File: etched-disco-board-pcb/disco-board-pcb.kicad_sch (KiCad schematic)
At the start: 15 parts, among them J1 Conn_02x32_Odd_Even, J2 Conn_02x32_Odd_Even, U2 MMA8452Q

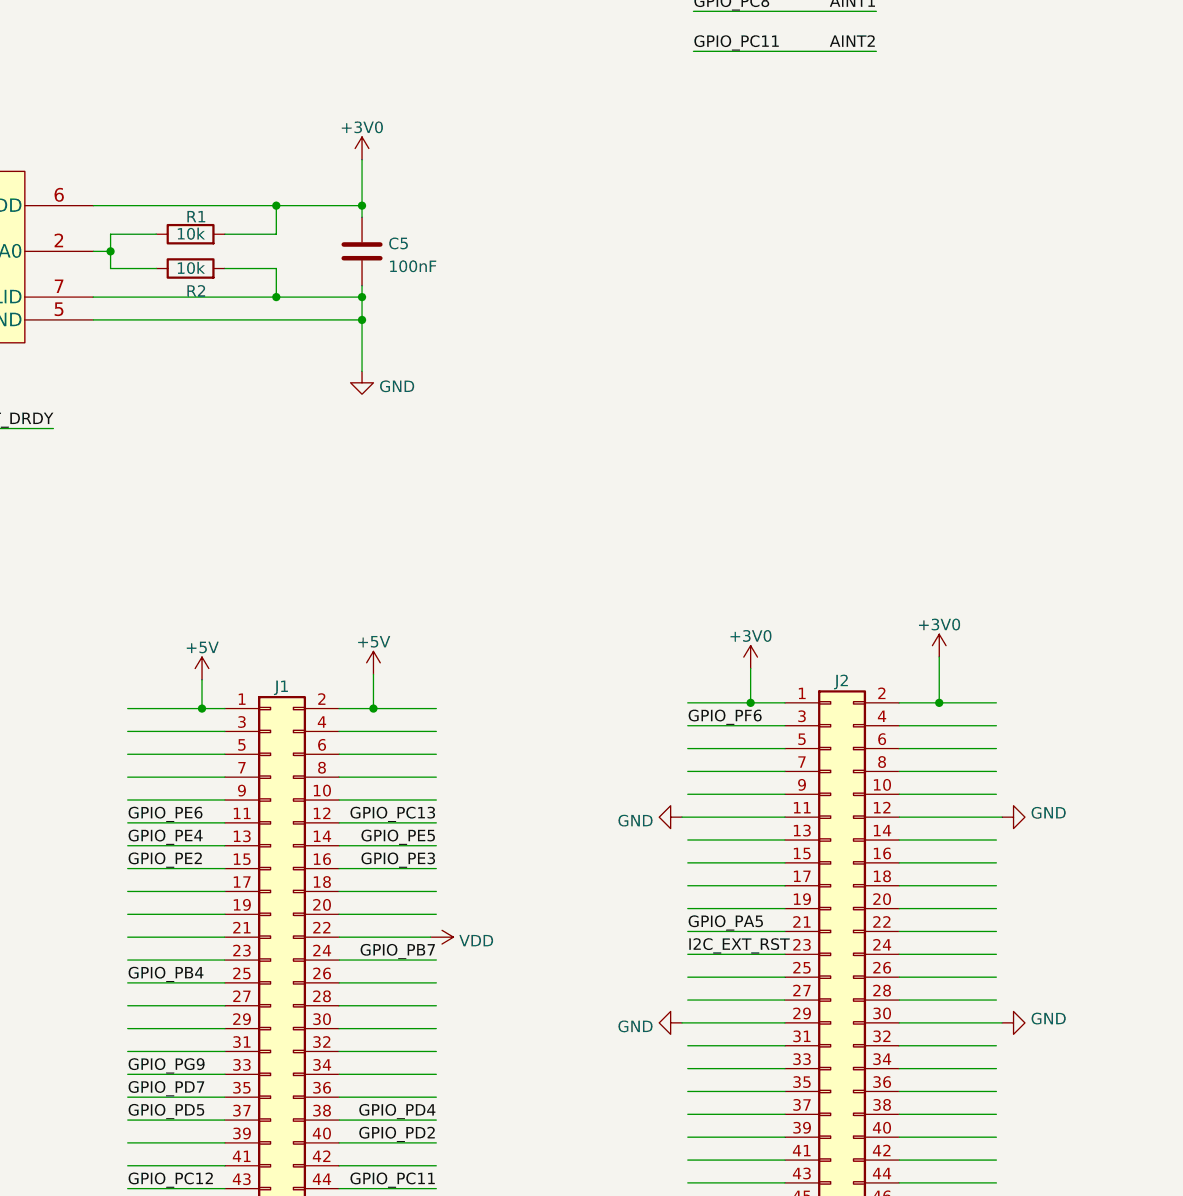
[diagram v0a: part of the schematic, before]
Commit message: Correcting error in PCB where NRST was connected to GND on etched-disco-board-pcb
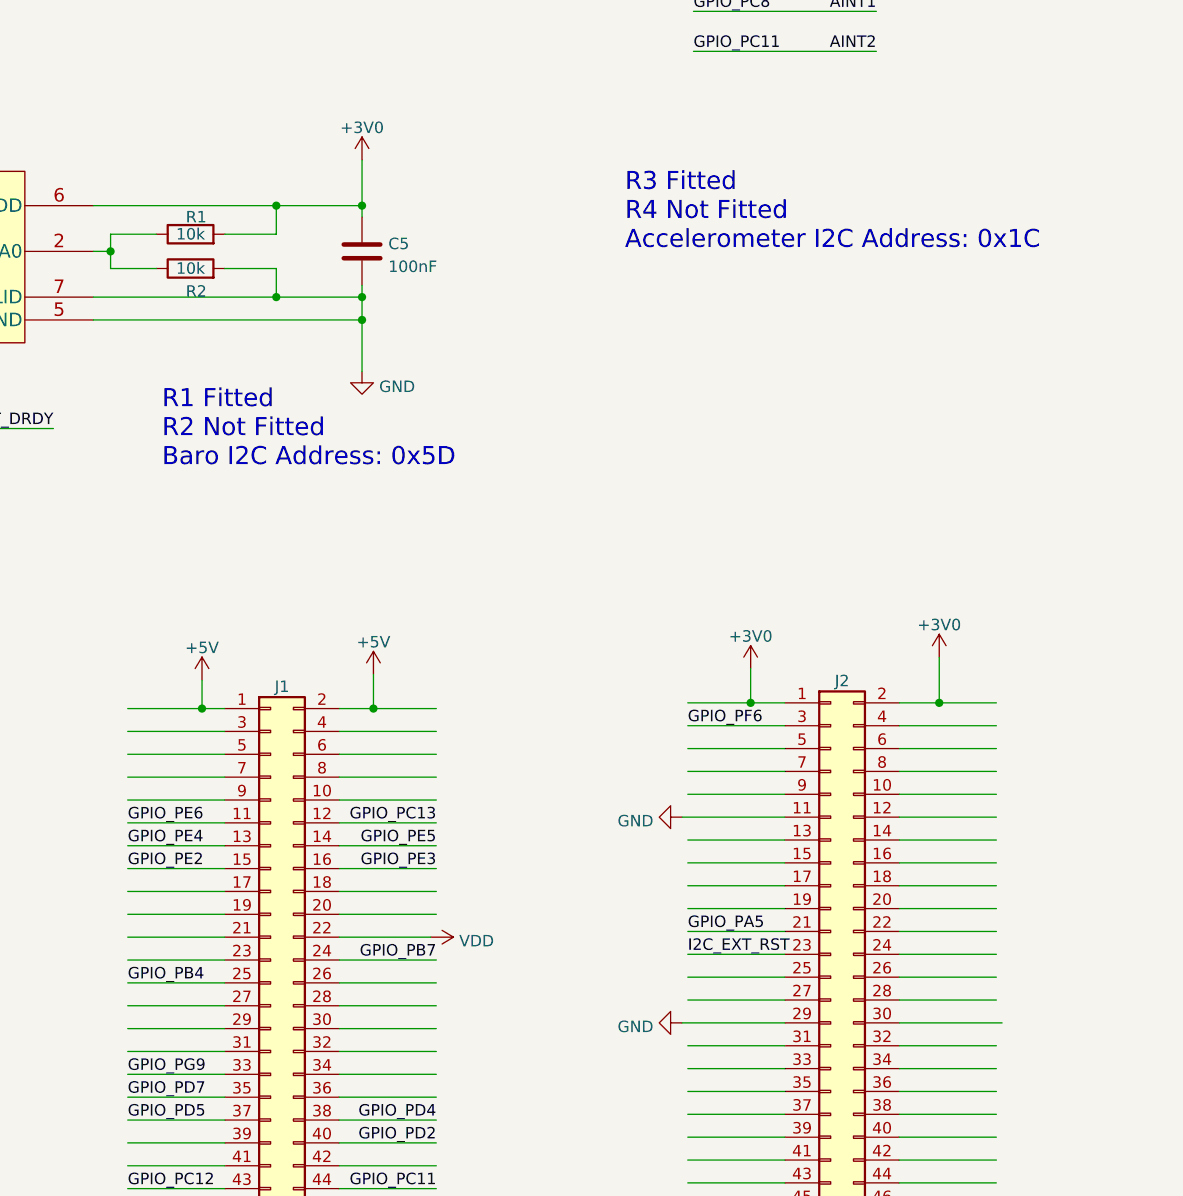
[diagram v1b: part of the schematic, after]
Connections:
- net GND: no longer J2.12 (Pin_12), J2.30 (Pin_30)
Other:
- note added: "R1 Fitted R2 Not Fitted Baro I2C Address: 0x5D"
- note added: "R3 Fitted R4 Not Fitted Accelerometer I2C Address: 0x1C"
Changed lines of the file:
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@@
+    (stroke (width 0) (type default) (color 0 0 0 0))
+  )
+  (wire (pts (xy 165.1 177.8) (xy 175.895 177.8))
     (stroke (width 0) (type default) (color 0 0 0 0))
   )
@@
     (stroke (width 0) (type default) (color 0 0 0 0))
   )
-  (wire (pts (xy 165.1 177.8) (xy 176.53 177.8))
-    (stroke (width 0) (type default) (color 0 0 0 0))
-  )
   (wire (pts (xy 79.375 180.975) (xy 90.17 180.975))
     (stroke (width 0) (type default) (color 0 0 0 0))
@@
   (wire (pts (xy 137.795 69.215) (xy 143.51 69.215))
     (stroke (width 0) (type default) (color 0 0 0 0))
+  )
+  (text "R1 Fitted\nR2 Not Fitted\nBaro I2C Address: 0x5D" (at 83.185 139.065 0)
+    (effects (font (size 2 2)) (justify left bottom))
+  )
+  (text "R3 Fitted\nR4 Not Fitted\nAccelerometer I2C Address: 0x1C"
+    (at 134.62 114.935 0)
+    (effects (font (size 2 2)) (justify left bottom))
   )
   (label "INT_DRDY" (at 71.12 134.62 180)
@@
     (pin "1")
   )
-  (symbol (lib_id "power:GND") (at 176.53 200.66 90) (unit 1)
-    (in_bom yes) (on_board yes) (fields_autoplaced)
-    (property "Reference" "#PWR017" (id 0) (at 182.88 200.66 0)
-      (effects (font (size 1.27 1.27)) hide)
-    )
-    (property "Value" "GND" (id 1) (at 179.7049 200.2262 90)
-      (effects (font (size 1.27 1.27)) (justify right))
-    )
-    (property "Footprint" "" (id 2) (at 176.53 200.66 0)
-      (effects (font (size 1.27 1.27)) hide)
-    )
-    (property "Datasheet" "" (id 3) (at 176.53 200.66 0)
-      (effects (font (size 1.27 1.27)) hide)
-    )
-    (pin "1")
-  )
   (symbol (lib_id "Device:C") (at 121.92 57.15 0) (unit 1)
     (in_bom yes) (on_board yes)
@@
     (property "Datasheet" "" (id 3) (at 89.535 51.435 0)
       (effects (font (size 1.524 1.524)))
-    )
-    (pin "1")
-  )
-  (symbol (lib_id "power:GND") (at 176.53 177.8 90) (unit 1)
-    (in_bom yes) (on_board yes) (fields_autoplaced)
-    (property "Reference" "#PWR016" (id 0) (at 182.88 177.8 0)
-      (effects (font (size 1.27 1.27)) hide)
-    )
-    (property "Value" "GND" (id 1) (at 179.7049 177.3662 90)
-      (effects (font (size 1.27 1.27)) (justify right))
-    )
-    (property "Footprint" "" (id 2) (at 176.53 177.8 0)
-      (effects (font (size 1.27 1.27)) hide)
-    )
-    (property "Datasheet" "" (id 3) (at 176.53 177.8 0)
-      (effects (font (size 1.27 1.27)) hide)
     )
     (pin "1")
@@
       (reference "#PWR015") (unit 1) (value "+3V0") (footprint "")
     )
-    (path "/6d990687-4293-4f07-8f96-f287a03edb80"
-      (reference "#PWR016") (unit 1) (value "GND") (footprint "")
-    )
-    (path "/4cef86db-de30-4bd5-a76d-93c6d623e5cc"
-      (reference "#PWR017") (unit 1) (value "GND") (footprint "")
-    )
     (path "/0651d730-ecb9-40ff-b7da-0ec46119c541"
